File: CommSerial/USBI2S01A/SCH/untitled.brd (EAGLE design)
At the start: 40.1 x 40.1 mm, 32 parts, among them P1 750mA, X1 CP2114, X4 SROUB3M, X5 SROUB3M, X6 SROUB3M, X7 SROUB3M

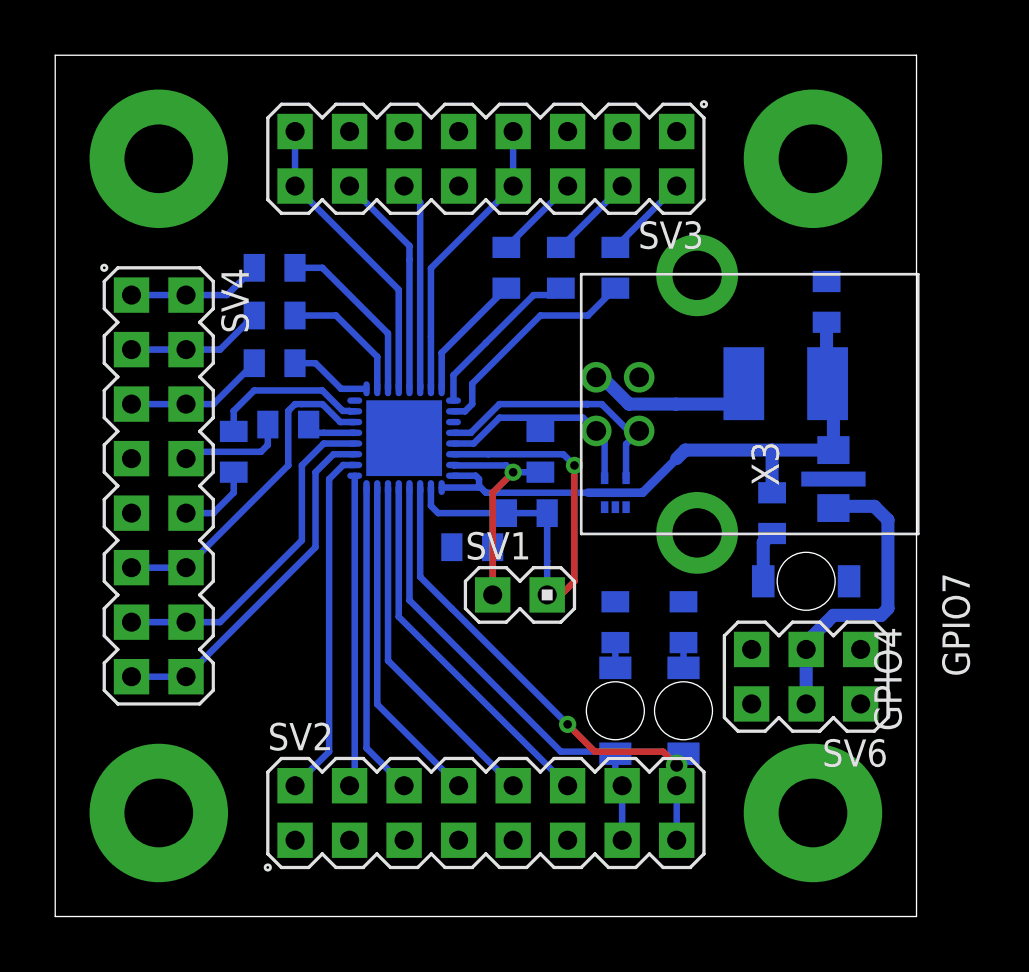
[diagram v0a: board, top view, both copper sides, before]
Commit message: 
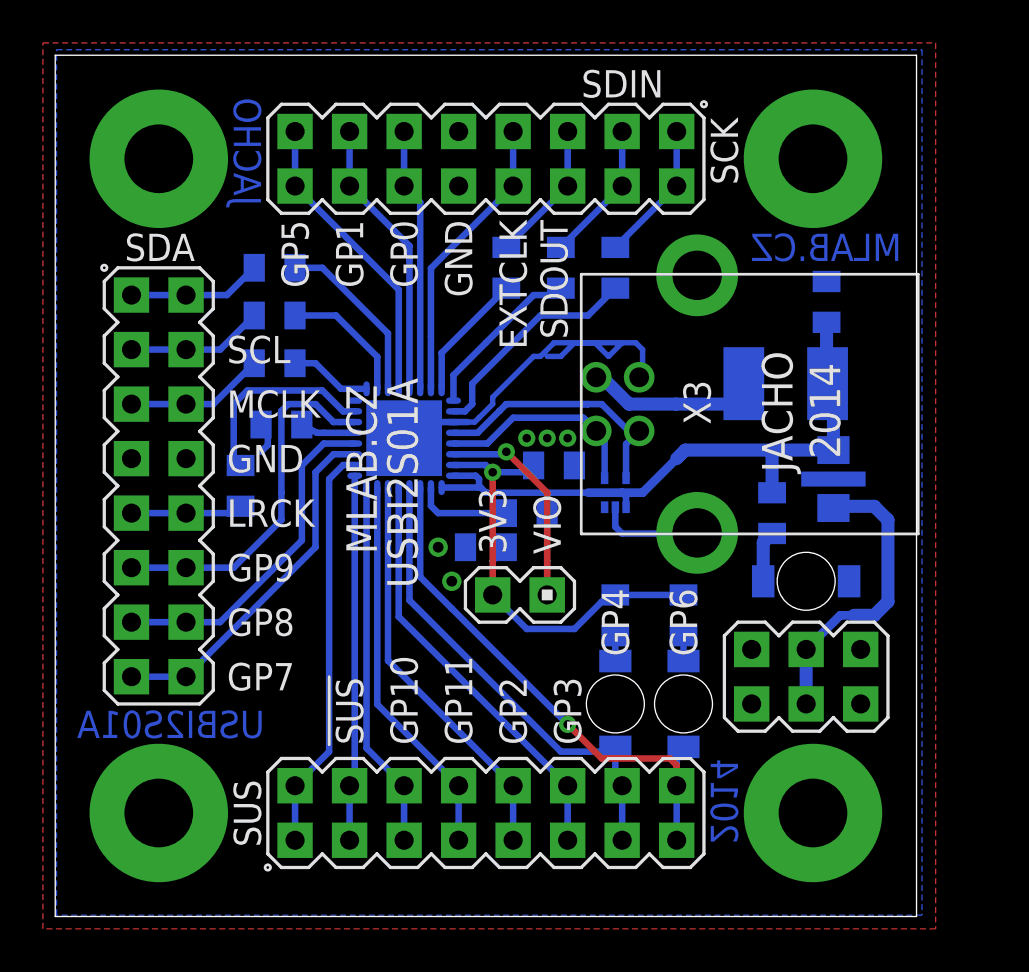
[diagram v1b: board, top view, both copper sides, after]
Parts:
- moved R12 1.62 mm to (8.89, 20.3)
- moved C2 0.90 mm to (23.5, 21.3), turned to 180 degrees
- moved C3 0.64 mm to (20.3, 17.5)
- moved C5 0.32 mm to (10.8, 23.2)
- moved D2 0.32 mm to (29.5, 10.2)
- moved D5 0.32 mm to (26.4, 10.2)
- moved R2 0.32 mm to (26.4, 14.3)
- moved R4 0.32 mm to (29.5, 14.3)
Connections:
- net N$14 renamed SUSPEND
- net N$16 renamed GP9
- net N$17 renamed /SUSPEND
- net N$18 renamed GP10
- net N$19 renamed GP11
- net N$20 renamed GP2
- net N$21 renamed GP3
- net N$22 renamed GP4
- net N$23 renamed GP6
- net N$24 renamed SCK
- net N$25 renamed SDIN
- net N$26 renamed SDOUT
- net N$27 renamed GP5
- net N$28 renamed GP1
- net N$29 renamed GP0
- net N$30 renamed EXTCLK
- net N$38 renamed GP08
- net N$39 renamed GP7
- net N$40 renamed SDA
- net N$41 renamed SCL
- net N$42 renamed MCLK
- net N$43 renamed LRCK
- net N$7 renamed VIO
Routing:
- net GND: track 5.03 -> 25.5 mm, vias 0 -> 5
- net +3.3V: track 12.5 -> 22.8 mm
- net VIO: track 16.6 -> 13.8 mm
- net /SUSPEND: track 14.5 -> 17.1 mm
- net SUSPEND: track 16.4 -> 18.9 mm
- net SDOUT: track 4.04 -> 6.58 mm
- net SDIN: track 4.04 -> 6.58 mm
- net SCK: track 4.04 -> 6.58 mm
- net GP3: track 17.2 -> 19.7 mm
- net GP2: track 16.3 -> 18.8 mm
- net GP11: track 15.5 -> 18.0 mm
- net GP10: track 14.6 -> 17.2 mm
- net GP1: track 10.6 -> 13.1 mm
- net GP0: track 9.76 -> 12.3 mm
- net N$37: track 7.39 -> 9.74 mm
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- added copper zone on layer 1, net GND
- added copper zone on layer 16, net GND
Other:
- board text added: "2014"
- board text added: "3V3"
- board text added: "EXTCLK"
- board text added: "GND"
- board text added: "GP0"
- board text added: "GP1"
- board text added: "GP10"
- board text added: "GP11"
- board text added: "GP2"
- board text added: "GP3"
- board text added: "GP4"
- board text added: "GP5"
- board text added: "GP6"
- board text added: "GP7"
- board text added: "GP8"
- board text added: "GP9"
- board text added: "JACHO"
- board text added: "LRCK"
- board text added: "MCLK"
- board text added: "MLAB.CZ"
- board text added: "SCK"
- board text added: "SCL"
- board text added: "SDA"
- board text added: "SDIN"
- board text added: "SDOUT"
- board text added: "SUS"
- board text added: "USBI2S01A"
- board text added: "VIO"
- board text removed: "GPIO4"
- board text removed: "GPIO7"
